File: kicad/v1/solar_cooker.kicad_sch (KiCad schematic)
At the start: 10 parts, among them SW1 SW_DPST_x2, U1 ATmega2560-16A, U2 microSD, U3 clock_module, U4 e-Paper, U5 anemometer, U6 BME680, U7 PT100, U8 GPS

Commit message: KiCad v2 update
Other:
- moved on the sheet: R1, SW1A, U1, U2, U3, U4, U5, U6, U7, U8

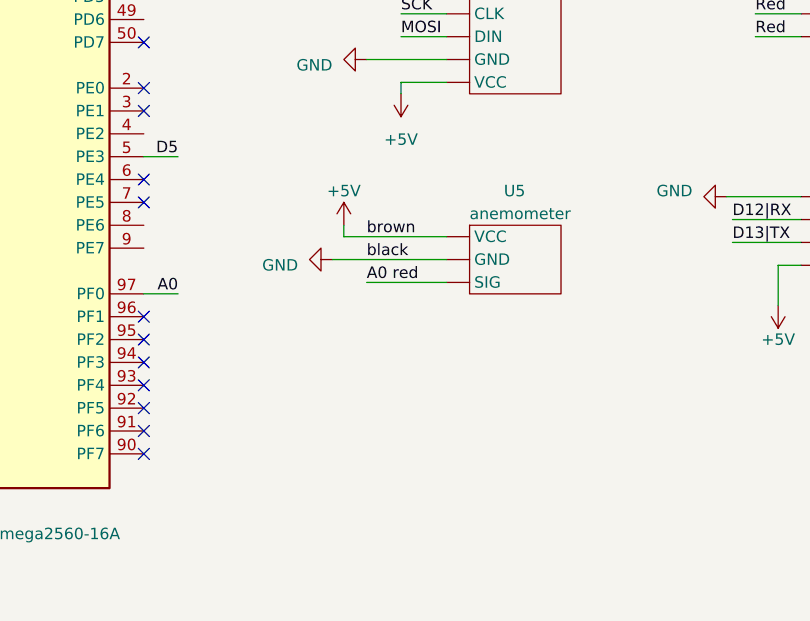
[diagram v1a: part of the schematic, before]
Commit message: update main + added schematic AM2315
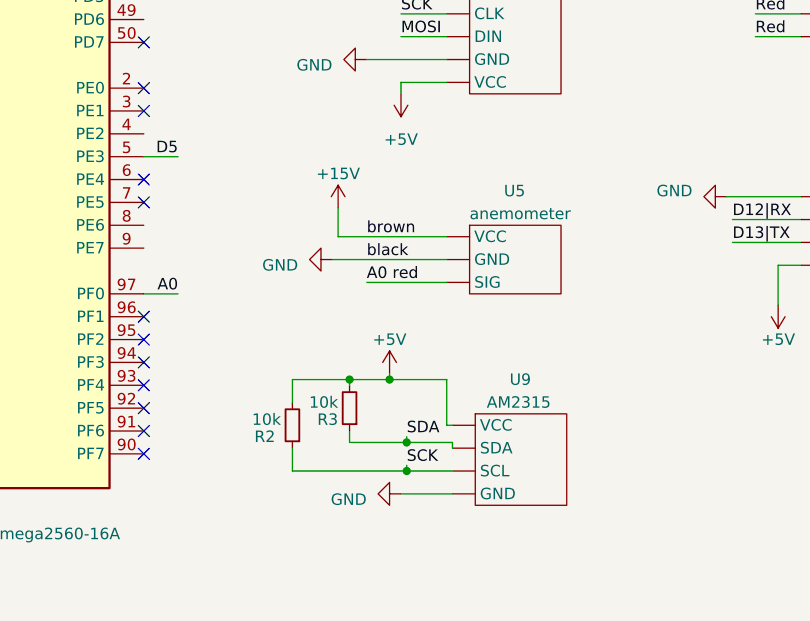
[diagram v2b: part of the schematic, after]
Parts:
- added R2, R3: 10k, symbol Device:R_Small
- added U9: AM2315, symbol custom_components:AM2315
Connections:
- net +5V: now also R2.2, R3.2, U9.1 (VCC); no longer U5.1 (VCC)
- net GND: now also U9.4 (GND)
- net SCK: now also R2.1, U9.3 (SCL)
- net SDA: now also R3.1, U9.2 (SDA)
- new net +15V: U5.1 (VCC)
